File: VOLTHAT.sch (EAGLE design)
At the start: 15 parts, among them J1 M40-SOCKET-BELOW, J2 DC IN, J4 DC IN, J5 OLED, J7 M14PTH, J8 M06-PLAIN, J9 M06-PLAIN

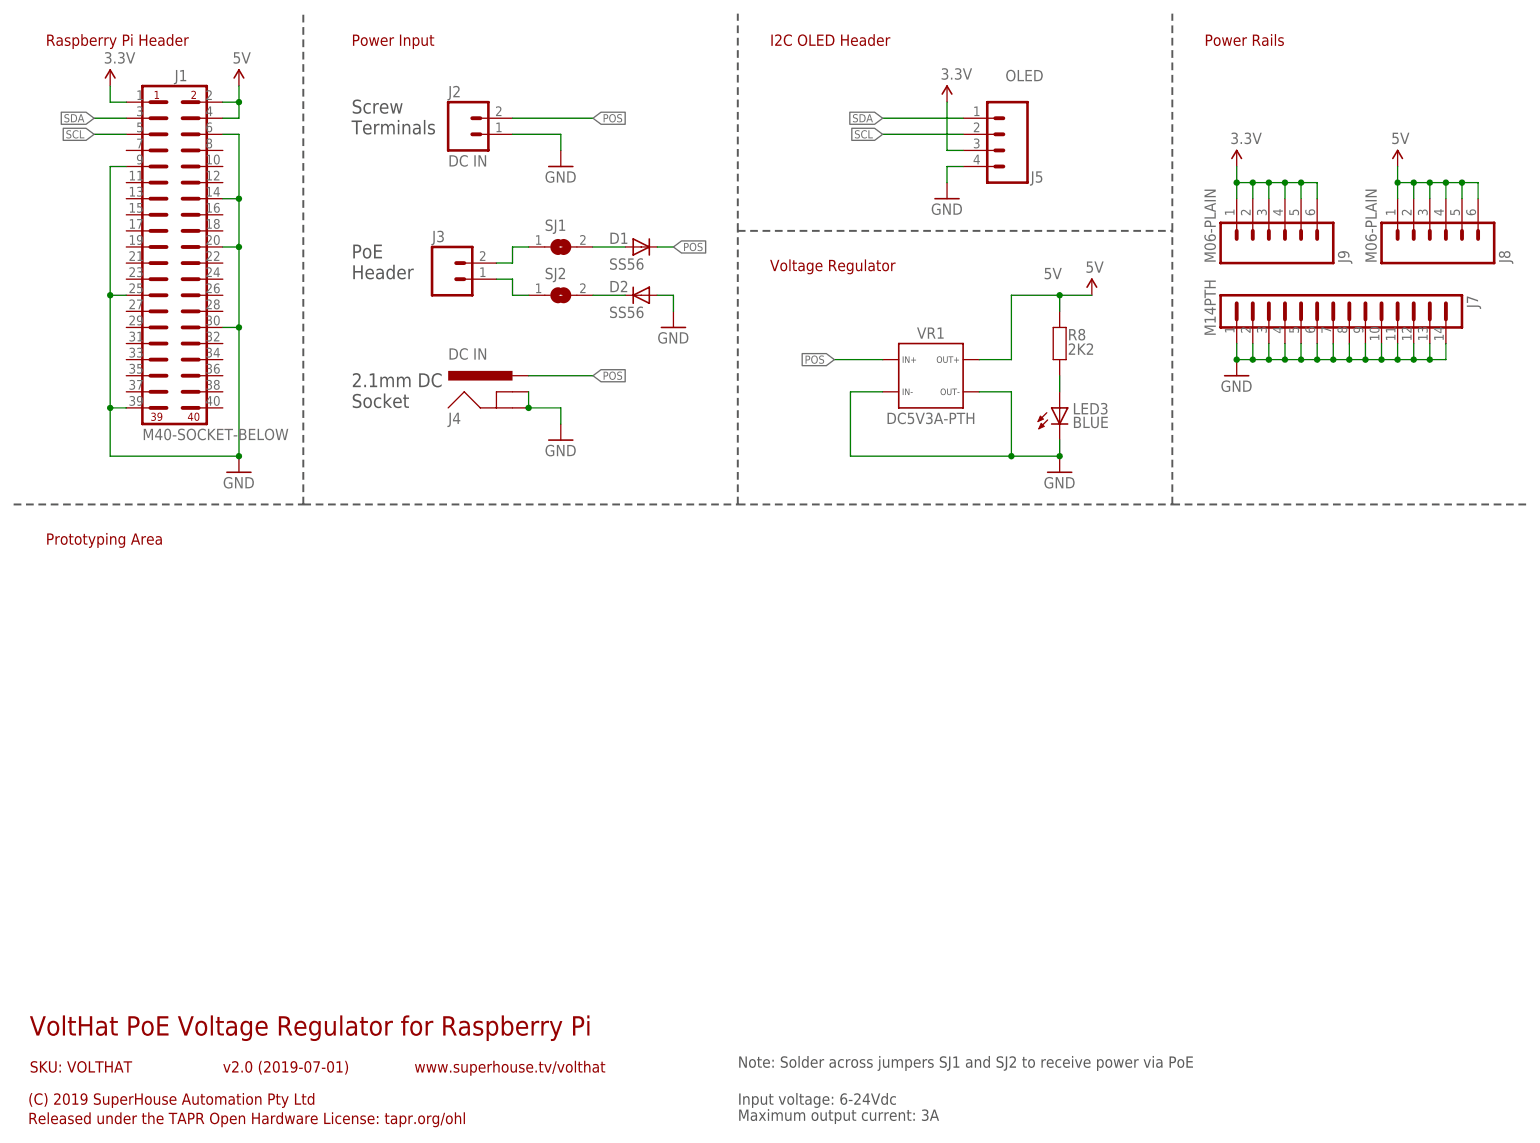
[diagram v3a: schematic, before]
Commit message: Added I2C-BREAKOUT header for v3.0 release
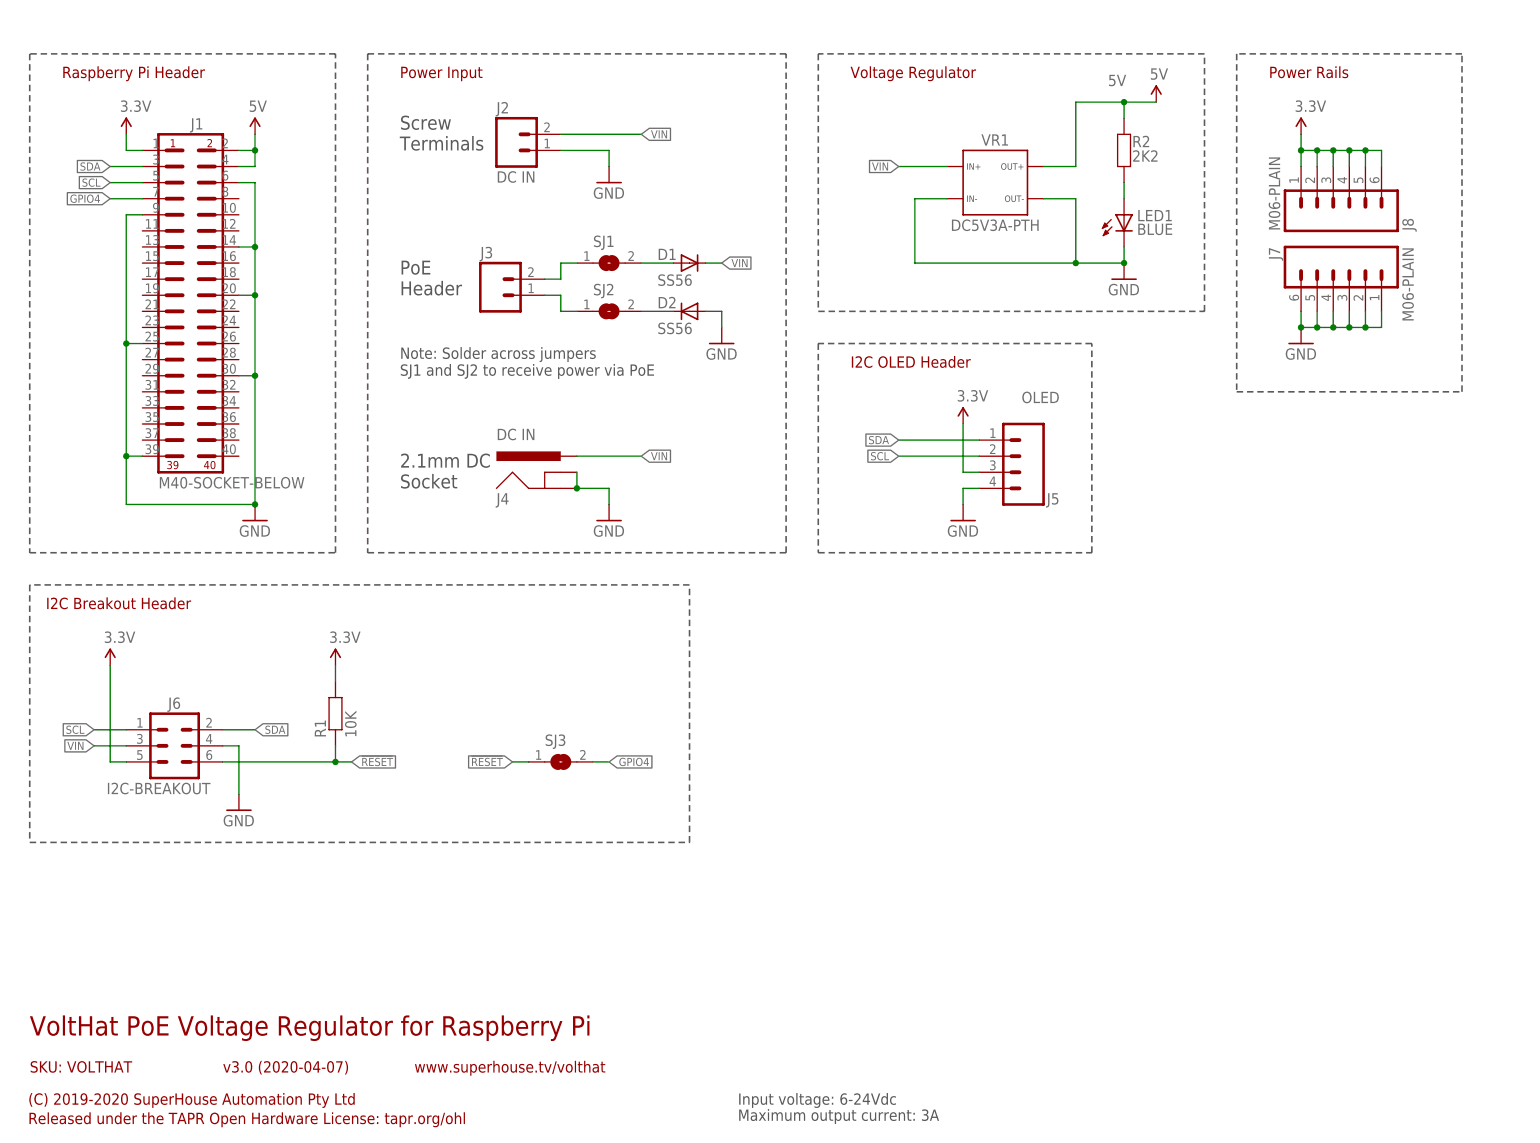
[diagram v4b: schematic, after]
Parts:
- removed J9: M06-PLAIN, SuperHouse-Connectors:M06-PLAIN
- removed LED3: BLUE, SuperHouse-LEDs:LED0603
- removed R8: 2K2, SuperHouse-DiscreteSemi:RESISTOR0603
- added J6: I2C-BREAKOUT, SuperHouse-Connectors:M02X3-SHROUDED
- added LED1: BLUE, SuperHouse-LEDs:LED0603
- added R1: 10K, SuperHouse-DiscreteSemi:RESISTOR0603
- added R2: 2K2, SuperHouse-DiscreteSemi:RESISTOR0603
- added SJ3: (no value), SuperHouse-Jumpers:SJ-NORMAL
- J7: value M14PTH -> M06-PLAIN; device freetronics-jon:M14PTH -> SuperHouse-Connectors:M06-PLAIN
- SJ1, SJ2: device freetronics-jon:SJN -> SuperHouse-Jumpers:SJ-NORMAL
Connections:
- removed net POS: D1.C, J2.2, J4.PWR, VR1.2
- new net !RESET: J6.6, R1.1, SJ3.1
- new net GPIO4: J1.7, SJ3.2
- new net VIN: D1.C, J2.2, J4.PWR, J6.3, VR1.2
- net 3.3V: now also J6.5, J8.1, J8.2, J8.3, J8.4, J8.5, J8.6, R1.2; no longer J9.1, J9.2, J9.3, J9.4, J9.5, J9.6
- net 5V: now also R2.1; no longer J8.1, J8.2, J8.3, J8.4, J8.5, J8.6, R8.1
- net GND: now also J6.4, LED1.C; no longer J7.10, J7.11, J7.12, J7.13, J7.14, J7.7, J7.8, J7.9, LED3.C
- net N$203: now also LED1.A, R2.2; no longer LED3.A, R8.2
- net SCL: now also J6.1
- net SDA: now also J6.2
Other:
- note added: "(C) 2019-2020 SuperHouse Automation Pty Ltd"
- note added: "I2C Breakout Header"
- note added: "v3.0 (2020-04-07)"
- note removed: "(C) 2019 SuperHouse Automation Pty Ltd"
- note removed: "Prototyping Area"
- note removed: "v2.0 (2019-07-01)"
- moved on the sheet: D1, D2, J1, J2, J3, J4, J5, J8, SJ1, SJ2, VR1
